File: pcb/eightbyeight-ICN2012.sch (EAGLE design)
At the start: 136 parts, among them CON1 USB_MICROSMT+THRUHULE, Q1 16MHz, SW1 SWITCH_SPDT, SW2 BRIGHTNESS, U1 MK20DN64VFM5, U2 ICN2026, U4 ICN2026, U5 MIC5219 3.3V, U6 ESP_WROOM_02, U8 MMA8653FC

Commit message: Update ICN2012 version with new accelerometer
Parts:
- removed C13: 100nF, adafruit:C-USC0402
- removed U$1: ICN2012, blinkinlabs:ICN2012
- added U3: QMA6981, DevicesToMerge:QMA6981
- R21: value 2k 1% -> 10k
- U1: value MK20DN64VFM5 -> MK20DN32VFM5
- U8: value MMA8653FC -> ICN2012; device teensy_adapter:MMA8653FC -> blinkinlabs:ICN2012
- renumbered BAT to J3, CON1 to J1, TP16 to TP1, U$2 to J2, U$8 to U7
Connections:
- removed net ACC_INT1: U6.IO13, U8.INT1
- removed net N$5: C13.1, U8.BYP
- new net ADC_INT1: U3.INT1, U6.IO13
- net +3V3: now also U3.VDD, U3.VDDIO; no longer U8.VDD, U8.VDDIO
- net +5V: now also U8.VDD; no longer U$1.VDD
- net 1ROW0: now also U8.OUT0; no longer U$1.OUT0
- net 1ROW1: now also U8.OUT1; no longer U$1.OUT1
- net 1ROW2: now also U8.OUT2; no longer U$1.OUT2
- net 1ROW3: now also U8.OUT3; no longer U$1.OUT3
- net 1ROW4: now also U8.OUT4; no longer U$1.OUT4
- net 1ROW5: now also U8.OUT5; no longer U$1.OUT5
- net 1ROW6: now also U8.OUT6; no longer U$1.OUT6
- net 1ROW7: now also U8.OUT7; no longer U$1.OUT7
- net GND: now also U3.AD0, U3.GND; no longer C13.2, U$1.GND
- net I2C_SCL: now also U3.SCL; no longer U8.SCL
- net I2C_SDA: now also U3.SDA; no longer U8.SDA
- net LED_HS_EN: now also U8.E1; no longer U$1.E1
- net LED_OE: now also U8.E2; no longer U$1.E2
- net LED_ROW_A: now also U8.A0; no longer U$1.A0
- net LED_ROW_B: now also U8.A1; no longer U$1.A1
- net LED_ROW_C: now also U8.A2; no longer U$1.A2
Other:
- note added: "Place near U2, U4 pin 24"
- note added: "Place near pin 1, 9"
- note removed: "Place near U2, U4"

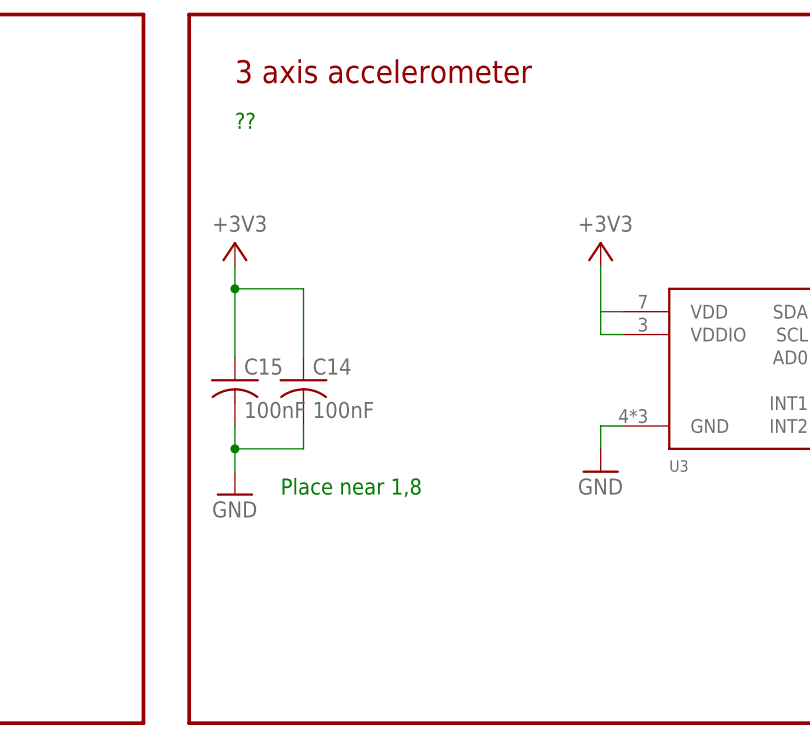
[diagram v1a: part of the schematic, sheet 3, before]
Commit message: Finish laying out accelerometer, minor updates to part values/reference designators
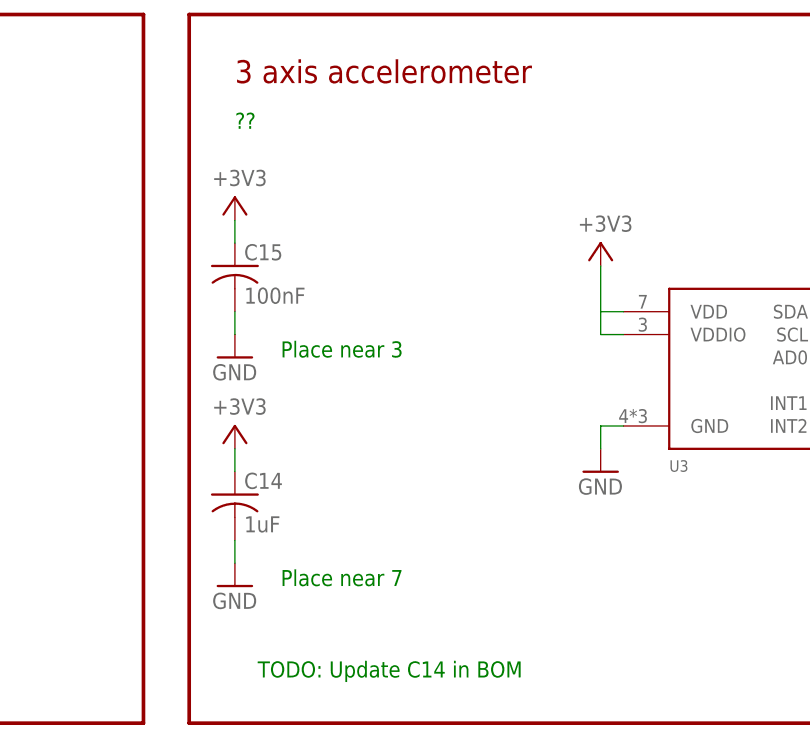
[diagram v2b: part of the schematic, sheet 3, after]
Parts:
- C14: value 100nF -> 1uF
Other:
- note added: "Place near 3"
- note added: "Place near 7"
- note added: "TODO: Update C14 in BOM"
- note removed: "Place near 1,8"
- moved on the sheet: C14, C15
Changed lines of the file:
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@@
 <part name="R17" library="adafruit" deviceset="R-US_" device="R0402" value="4.7k"/>
 <part name="R18" library="adafruit" deviceset="R-US_" device="R0402" value="4.7k"/>
-<part name="C14" library="adafruit" deviceset="C-US" device="C0402" value="100nF"/>
+<part name="C14" library="adafruit" deviceset="C-US" device="C0402" value="1uF"/>
 <part name="C15" library="adafruit" deviceset="C-US" device="C0402" value="100nF"/>
 <part name="GND32" library="SparkFun-Aesthetics" deviceset="GND" device=""/>
@@
 <part name="3V8" library="supply1" deviceset="+3V3" device=""/>
 <part name="GND47" library="SparkFun-Aesthetics" deviceset="GND" device=""/>
+<part name="3V1" library="supply1" deviceset="+3V3" device=""/>
+<part name="GND31" library="SparkFun-Aesthetics" deviceset="GND" device=""/>
 </parts>
 <sheets>
@@
 <wire x1="160.02" y1="91.44" x2="274.32" y2="91.44" width="0.4064" layer="94"/>
 <wire x1="274.32" y1="91.44" x2="274.32" y2="170.18" width="0.4064" layer="94"/>
-<text x="170.18" y="116.84" size="1.778" layer="91">Place near 1,8</text>
+<text x="170.18" y="132.08" size="1.778" layer="91">Place near 3</text>
 <text x="256.54" y="238.76" size="1.778" layer="91">Unused pins from the ESP8266</text>
 <text x="256.54" y="243.84" size="2.54" layer="94">Extra IO</text>
@@
 <wire x1="251.46" y1="175.26" x2="309.88" y2="175.26" width="0.4064" layer="94"/>
 <wire x1="309.88" y1="175.26" x2="309.88" y2="251.46" width="0.4064" layer="94"/>
+<text x="170.18" y="106.68" size="1.778" layer="91">Place near 7</text>
+<text x="167.64" y="96.52" size="1.778" layer="91">TODO: Update C14 in BOM</text>
 </plain>
 <instances>
@@
 <attribute name="VALUE" x="118.11" y="116.205" size="1.778" layer="96" rot="MR270"/>
 </instance>
-<instance part="C14" gate="G$1" x="172.72" y="129.54"/>
-<instance part="C15" gate="G$1" x="165.1" y="129.54"/>
-<instance part="GND32" gate="1" x="165.1" y="116.84"/>
+<instance part="C14" gate="G$1" x="165.1" y="116.84"/>
+<instance part="C15" gate="G$1" x="165.1" y="142.24"/>
+<instance part="GND32" gate="1" x="165.1" y="132.08"/>
 <instance part="R26" gate="G$1" x="43.18" y="220.98" smashed="yes" rot="R90">
 <attribute name="NAME" x="42.1894" y="215.392" size="1.778" layer="95" rot="R90"/>
@@
 <attribute name="VALUE" x="120.904" y="140.208" size="1.778" layer="96" rot="R90"/>
 </instance>
-<instance part="3V4" gate="G$1" x="165.1" y="144.78" smashed="yes">
-<attribute name="VALUE" x="162.56" y="146.05" size="1.778" layer="96"/>
+<instance part="3V4" gate="G$1" x="165.1" y="149.86" smashed="yes">
+<attribute name="VALUE" x="162.56" y="151.13" size="1.778" layer="96"/>
 </instance>
 <instance part="3V6" gate="G$1" x="121.92" y="147.32" smashed="yes">
@@
 </instance>
 <instance part="GND47" gate="1" x="238.76" y="119.38"/>
+<instance part="3V1" gate="G$1" x="165.1" y="124.46" smashed="yes">
+<attribute name="VALUE" x="162.56" y="125.73" size="1.778" layer="96"/>
+</instance>
+<instance part="GND31" gate="1" x="165.1" y="106.68"/>
 </instances>
 <busses>
@@
 <segment>
 <pinref part="C14" gate="G$1" pin="2"/>
-<wire x1="172.72" y1="121.92" x2="172.72" y2="124.46" width="0.1524" layer="91"/>
-<wire x1="165.1" y1="121.92" x2="172.72" y2="121.92" width="0.1524" layer="91"/>
+<wire x1="165.1" y1="109.22" x2="165.1" y2="111.76" width="0.1524" layer="91"/>
+<pinref part="GND31" gate="1" pin="GND"/>
+</segment>
+<segment>
 <pinref part="C15" gate="G$1" pin="2"/>
-<wire x1="165.1" y1="124.46" x2="165.1" y2="121.92" width="0.1524" layer="91"/>
-<junction x="165.1" y="121.92"/>
 <pinref part="GND32" gate="1" pin="GND"/>
-<wire x1="165.1" y1="119.38" x2="165.1" y2="121.92" width="0.1524" layer="91"/>
+<wire x1="165.1" y1="134.62" x2="165.1" y2="137.16" width="0.1524" layer="91"/>
 </segment>
 <segment>
@@
 <segment>
 <pinref part="C14" gate="G$1" pin="1"/>
-<wire x1="172.72" y1="139.7" x2="172.72" y2="132.08" width="0.1524" layer="91"/>
-<wire x1="172.72" y1="139.7" x2="165.1" y2="139.7" width="0.1524" layer="91"/>
+<pinref part="3V1" gate="G$1" pin="+3V3"/>
+<wire x1="165.1" y1="121.92" x2="165.1" y2="119.38" width="0.1524" layer="91"/>
+</segment>
+<segment>
 <pinref part="C15" gate="G$1" pin="1"/>
-<wire x1="165.1" y1="132.08" x2="165.1" y2="139.7" width="0.1524" layer="91"/>
-<wire x1="165.1" y1="142.24" x2="165.1" y2="139.7" width="0.1524" layer="91"/>
-<junction x="165.1" y="139.7"/>
+<wire x1="165.1" y1="144.78" x2="165.1" y2="147.32" width="0.1524" layer="91"/>
 <pinref part="3V4" gate="G$1" pin="+3V3"/>
 </segment>
